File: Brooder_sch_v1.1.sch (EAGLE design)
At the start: 31 parts, among them J1 DCJ0202, J2 1X2-3.5MM, J3 DCJ0202, J4 1X2-3.5MM, U1 328P

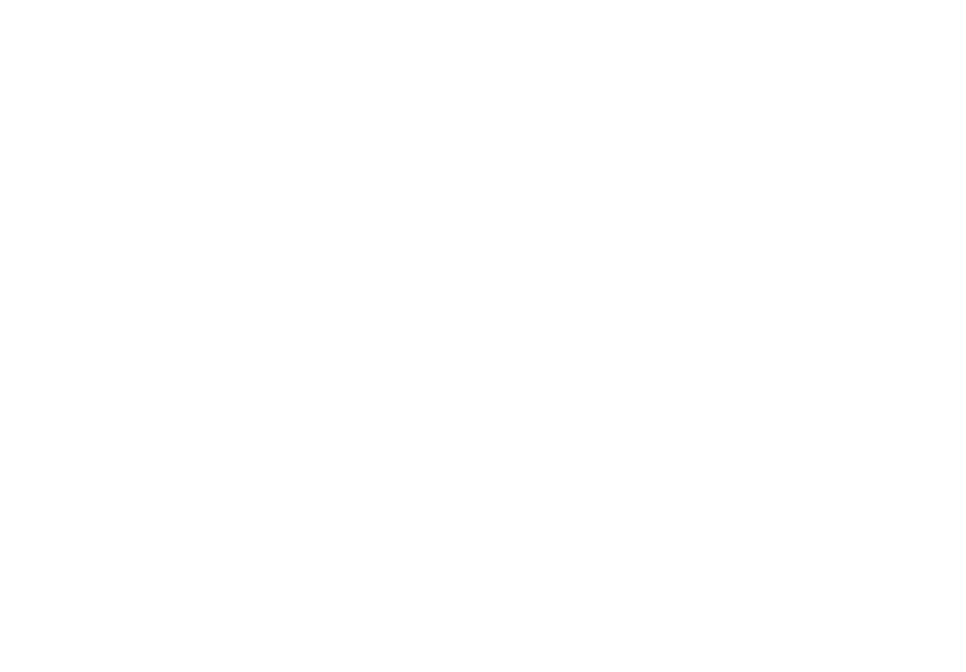
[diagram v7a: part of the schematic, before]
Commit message: Adds extractor fan relay to schematic
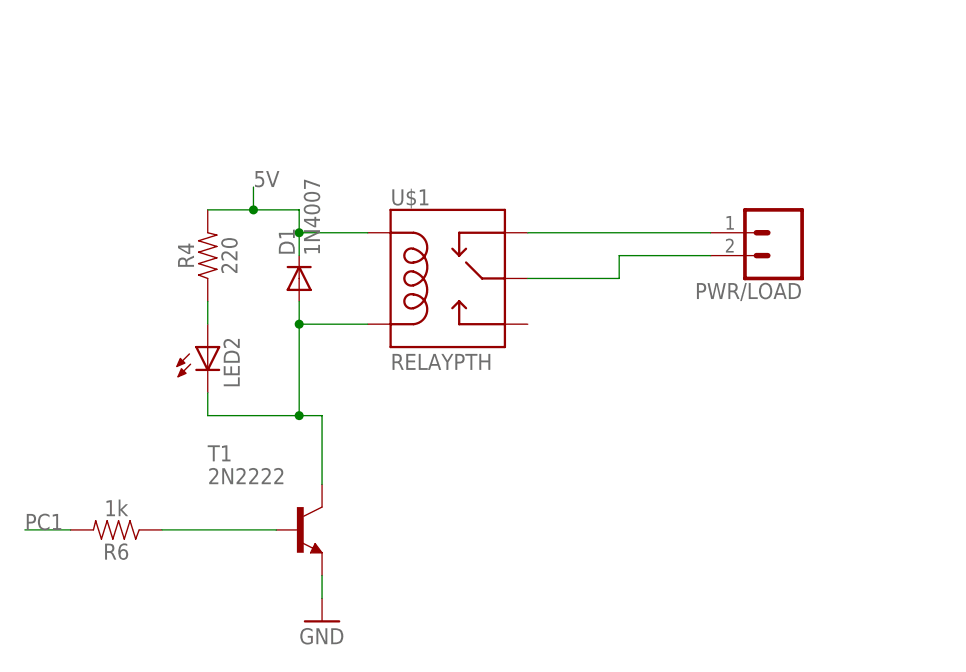
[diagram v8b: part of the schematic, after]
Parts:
- added D1: 1N4007, adafruit:1N4004
- added LED2: (no value), adafruit:LED5MM
- added PWR/LOAD: (no value), SparkFun-Connectors:CONN_025MM
- added R4: 220, SparkFun-Resistors:10MOHM-HORIZ-1/4W-5%
- added R6: 1k, SparkFun-Resistors:10MOHM-HORIZ-1/4W-5%
- added T1: 2N2222, adafruit:2N2222
- added U$1: RELAYPTH, SRD-05VDC-SL-C:RELAYPTH
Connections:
- new net N$10: R6.1, T1.B
- new net N$13: PWR/LOAD.1, U$1.SWCLOSE
- new net N$14: PWR/LOAD.2, U$1.SWCOMMON
- new net N$6: D1.A, LED2.C, T1.C, U$1.COIL0
- new net N$7: LED2.A, R4.1
- net 5V: now also D1.C, R4.2, U$1.COIL1
- net GND: now also T1.E
- net PC1: now also R6.2
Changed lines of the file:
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@@
 <part name="GND21" library="supply1" library_urn="urn:adsk.eagle:library:371" deviceset="GND" device=""/>
 <part name="JP1" library="pinhead" library_urn="urn:adsk.eagle:library:325" deviceset="PINHD-2X3" device="" package3d_urn="urn:adsk.eagle:package:22462/2"/>
+<part name="U$1" library="SRD-05VDC-SL-C" deviceset="RELAY" device="PTH"/>
+<part name="D1" library="adafruit" deviceset="1N4004" device="" value="1N4007"/>
+<part name="T1" library="adafruit" deviceset="2N2222" device=""/>
+<part name="PWR/LOAD" library="SparkFun-Connectors" deviceset="CONN_02" device="5MM"/>
+<part name="R4" library="SparkFun-Resistors" deviceset="10MOHM" device="-HORIZ-1/4W-5%" value="220"/>
+<part name="R6" library="SparkFun-Resistors" deviceset="10MOHM" device="-HORIZ-1/4W-5%" value="1k"/>
+<part name="LED2" library="adafruit" deviceset="LED" device="5MM"/>
+<part name="GND22" library="supply1" library_urn="urn:adsk.eagle:library:371" deviceset="GND" device=""/>
 </parts>
 <sheets>
@@
 </instance>
 <instance part="JP1" gate="A" x="154.94" y="-12.7"/>
+<instance part="U$1" gate="G$1" x="-27.94" y="-5.08" smashed="yes">
+<attribute name="NAME" x="-35.56" y="3.048" size="1.778" layer="95"/>
+<attribute name="VALUE" x="-35.56" y="-15.24" size="1.778" layer="96"/>
+</instance>
+<instance part="D1" gate="1" x="-45.72" y="-5.08" smashed="yes" rot="R90">
+<attribute name="NAME" x="-46.2026" y="-2.54" size="1.778" layer="95" rot="R90"/>
+<attribute name="VALUE" x="-43.4086" y="-2.54" size="1.778" layer="96" rot="R90"/>
+</instance>
+<instance part="T1" gate="G$1" x="-45.72" y="-33.02" smashed="yes">
+<attribute name="NAME" x="-55.88" y="-25.4" size="1.778" layer="95"/>
+<attribute name="VALUE" x="-55.88" y="-27.94" size="1.778" layer="96"/>
+</instance>
+<instance part="PWR/LOAD" gate="G$1" x="7.62" y="0" smashed="yes" rot="R180">
+<attribute name="VALUE" x="10.16" y="4.826" size="1.778" layer="96" font="vector" rot="R180"/>
+<attribute name="NAME" x="10.16" y="-5.588" size="1.778" layer="95" font="vector" rot="R180"/>
+</instance>
+<instance part="R4" gate="G$1" x="-55.88" y="-2.54" smashed="yes" rot="R90">
+<attribute name="NAME" x="-57.404" y="-2.54" size="1.778" layer="95" font="vector" rot="R90" align="bottom-center"/>
+<attribute name="VALUE" x="-54.356" y="-2.54" size="1.778" layer="96" font="vector" rot="R90" align="top-center"/>
+</instance>
+<instance part="R6" gate="G$1" x="-66.04" y="-33.02" smashed="yes" rot="R180">
+<attribute name="NAME" x="-66.04" y="-34.544" size="1.778" layer="95" font="vector" rot="R180" align="bottom-center"/>
+<attribute name="VALUE" x="-66.04" y="-31.496" size="1.778" layer="96" font="vector" rot="R180" align="top-center"/>
+</instance>
+<instance part="LED2" gate="G$1" x="-55.88" y="-12.7" smashed="yes">
+<attribute name="NAME" x="-52.324" y="-17.272" size="1.778" layer="95" rot="R90"/>
+<attribute name="VALUE" x="-50.165" y="-17.272" size="1.778" layer="96" rot="R90"/>
+</instance>
+<instance part="GND22" gate="1" x="-43.18" y="-43.18" smashed="yes">
+<attribute name="VALUE" x="-45.72" y="-45.72" size="1.778" layer="96"/>
+</instance>
 </instances>
 <busses>
@@
 <wire x1="160.02" y1="-15.24" x2="167.64" y2="-15.24" width="0.1524" layer="91"/>
 <label x="167.64" y="-15.24" size="1.778" layer="95"/>
+</segment>
+<segment>
+<pinref part="T1" gate="G$1" pin="E"/>
+<wire x1="-43.18" y1="-38.1" x2="-43.18" y2="-40.64" width="0.1524" layer="91"/>
+<pinref part="GND22" gate="1" pin="GND"/>
 </segment>
 </net>
@@
 <label x="167.64" y="-10.16" size="1.778" layer="95"/>
 </segment>
+<segment>
+<pinref part="U$1" gate="G$1" pin="COIL1"/>
+<pinref part="D1" gate="1" pin="C"/>
+<wire x1="-38.1" y1="0" x2="-45.72" y2="0" width="0.1524" layer="91"/>
+<wire x1="-45.72" y1="0" x2="-45.72" y2="-2.54" width="0.1524" layer="91"/>
+<pinref part="R4" gate="G$1" pin="2"/>
+<wire x1="-45.72" y1="0" x2="-45.72" y2="2.54" width="0.1524" layer="91"/>
+<wire x1="-45.72" y1="2.54" x2="-50.8" y2="2.54" width="0.1524" layer="91"/>
+<junction x="-45.72" y="0"/>
+<wire x1="-50.8" y1="2.54" x2="-55.88" y2="2.54" width="0.1524" layer="91"/>
+<wire x1="-50.8" y1="2.54" x2="-50.8" y2="5.08" width="0.1524" layer="91"/>
+<junction x="-50.8" y="2.54"/>
+<label x="-50.8" y="5.08" size="1.778" layer="95"/>
+</segment>
 </net>
 <net name="N$5" class="0">
@@
 <label x="93.98" y="15.24" size="1.778" layer="95"/>
 </segment>
+<segment>
+<pinref part="R6" gate="G$1" pin="2"/>
+<wire x1="-71.12" y1="-33.02" x2="-76.2" y2="-33.02" width="0.1524" layer="91"/>
+<label x="-76.2" y="-33.02" size="1.778" layer="95"/>
+</segment>
 </net>
 <net name="PC4" class="0">
@@
 </segment>
 </net>
+<net name="N$6" class="0">
+<segment>
+<pinref part="D1" gate="1" pin="A"/>
+<pinref part="U$1" gate="G$1" pin="COIL0"/>
+<wire x1="-45.72" y1="-7.62" x2="-45.72" y2="-10.16" width="0.1524" layer="91"/>
+<wire x1="-45.72" y1="-10.16" x2="-38.1" y2="-10.16" width="0.1524" layer="91"/>
+<pinref part="LED2" gate="G$1" pin="C"/>
+<wire x1="-55.88" y1="-17.78" x2="-55.88" y2="-20.32" width="0.1524" layer="91"/>
+<wire x1="-55.88" y1="-20.32" x2="-45.72" y2="-20.32" width="0.1524" layer="91"/>
+<wire x1="-45.72" y1="-20.32" x2="-45.72" y2="-10.16" width="0.1524" layer="91"/>
+<junction x="-45.72" y="-10.16"/>
+<pinref part="T1" gate="G$1" pin="C"/>
+<wire x1="-45.72" y1="-20.32" x2="-43.18" y2="-20.32" width="0.1524" layer="91"/>
+<wire x1="-43.18" y1="-20.32" x2="-43.18" y2="-27.94" width="0.1524" layer="91"/>
+<junction x="-45.72" y="-20.32"/>
+</segment>
+</net>
+<net name="N$7" class="0">
+<segment>
+<pinref part="R4" gate="G$1" pin="1"/>
+<pinref part="LED2" gate="G$1" pin="A"/>
+<wire x1="-55.88" y1="-7.62" x2="-55.88" y2="-10.16" width="0.1524" layer="91"/>
+</segment>
+</net>
+<net name="N$10" class="0">
+<segment>
+<pinref part="R6" gate="G$1" pin="1"/>
+<pinref part="T1" gate="G$1" pin="B"/>
+<wire x1="-60.96" y1="-33.02" x2="-48.26" y2="-33.02" width="0.1524" layer="91"/>
+</segment>
+</net>
+<net name="N$13" class="0">
+<segment>
+<pinref part="PWR/LOAD" gate="G$1" pin="1"/>
+<wire x1="-20.32" y1="0" x2="0" y2="0" width="0.1524" layer="91"/>
+<pinref part="U$1" gate="G$1" pin="SWCLOSE"/>
+</segment>
+</net>
+<net name="N$14" class="0">
+<segment>
+<pinref part="U$1" gate="G$1" pin="SWCOMMON"/>
+<pinref part="PWR/LOAD" gate="G$1" pin="2"/>
+<wire x1="0" y1="-2.54" x2="-10.16" y2="-2.54" width="0.1524" layer="91"/>
+<wire x1="-10.16" y1="-2.54" x2="-10.16" y2="-5.08" width="0.1524" layer="91"/>
+<wire x1="-10.16" y1="-5.08" x2="-20.32" y2="-5.08" width="0.1524" layer="91"/>
+</segment>
+</net>
